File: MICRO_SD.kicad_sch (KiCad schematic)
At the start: 9 parts, among them J15 TF-028-H265

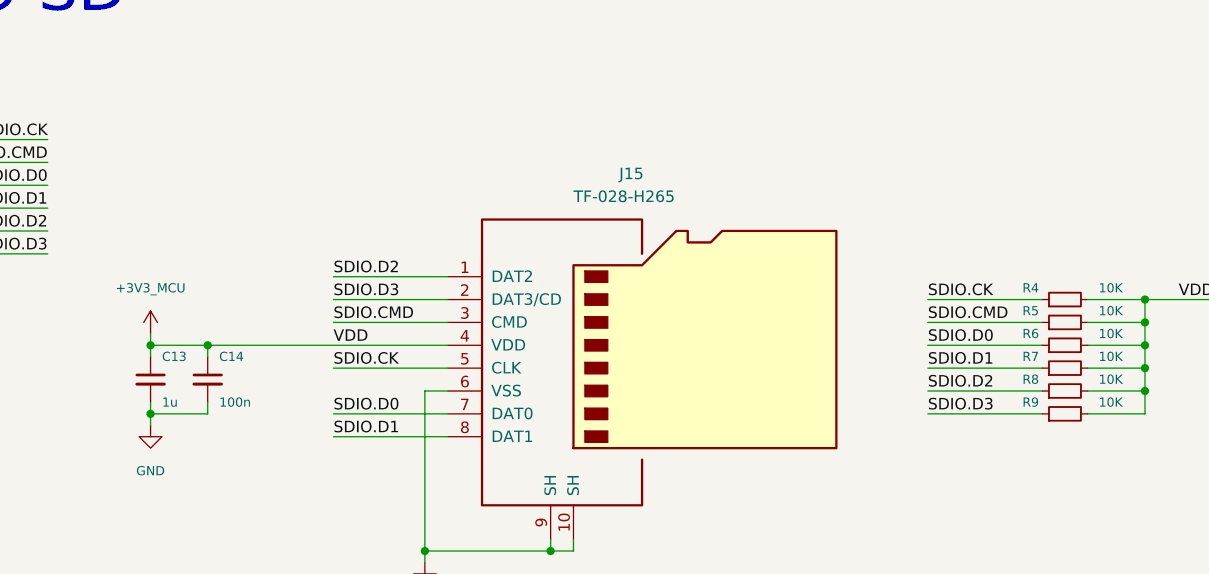
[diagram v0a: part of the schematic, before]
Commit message: grouped ICs and passives
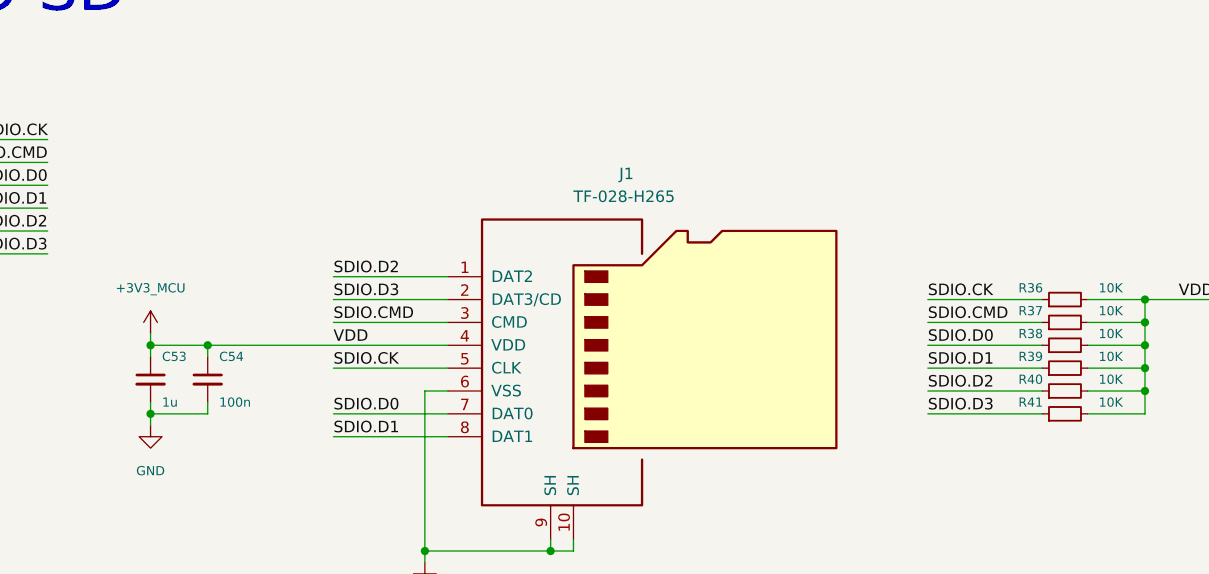
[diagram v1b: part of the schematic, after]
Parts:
- renumbered C13 to C53, C14 to C54, J15 to J1, R4 to R36, R5 to R37, R6 to R38, R7 to R39, R8 to R40, R9 to R41
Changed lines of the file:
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@@
 		(in_pos_files yes)
 		(dnp no)
-		(property "Reference" "R8"
+		(property "Reference" "R40"
 			(at 151.13 62.23 90)
 			(show_name no)
@@
 			(project "LEVIA_H7"
 				(path "/6b768b36-fce6-4be0-9021-6d41bddc3a70/f6fdd950-a71d-4aac-93a8-c5aad57c018b"
-					(reference "R8")
+					(reference "R40")
 					(unit 1)
 				)
@@
 		(in_pos_files yes)
 		(dnp no)
-		(property "Reference" "R7"
+		(property "Reference" "R39"
 			(at 151.13 59.69 90)
 			(show_name no)
@@
 			(project "LEVIA_H7"
 				(path "/6b768b36-fce6-4be0-9021-6d41bddc3a70/f6fdd950-a71d-4aac-93a8-c5aad57c018b"
-					(reference "R7")
+					(reference "R39")
 					(unit 1)
 				)
@@
 		(in_pos_files yes)
 		(dnp no)
-		(property "Reference" "R4"
+		(property "Reference" "R36"
 			(at 151.13 52.07 90)
 			(show_name no)
@@
 			(project "LEVIA_H7"
 				(path "/6b768b36-fce6-4be0-9021-6d41bddc3a70/f6fdd950-a71d-4aac-93a8-c5aad57c018b"
-					(reference "R4")
+					(reference "R36")
 					(unit 1)
 				)
@@
 		(dnp no)
 		(fields_autoplaced yes)
-		(property "Reference" "#PWR021"
+		(property "Reference" "#PWR0116"
 			(at 53.34 73.66 0)
 			(hide yes)
@@
 			(project "LEVIA_H7"
 				(path "/6b768b36-fce6-4be0-9021-6d41bddc3a70/f6fdd950-a71d-4aac-93a8-c5aad57c018b"
-					(reference "#PWR021")
+					(reference "#PWR0116")
 					(unit 1)
 				)
@@
 		(in_pos_files yes)
 		(dnp no)
-		(property "Reference" "R6"
+		(property "Reference" "R38"
 			(at 151.13 57.15 90)
 			(show_name no)
@@
 			(project "LEVIA_H7"
 				(path "/6b768b36-fce6-4be0-9021-6d41bddc3a70/f6fdd950-a71d-4aac-93a8-c5aad57c018b"
-					(reference "R6")
+					(reference "R38")
 					(unit 1)
 				)
@@
 		(in_pos_files yes)
 		(dnp no)
-		(property "Reference" "R5"
+		(property "Reference" "R37"
 			(at 151.13 54.61 90)
 			(show_name no)
@@
 			(project "LEVIA_H7"
 				(path "/6b768b36-fce6-4be0-9021-6d41bddc3a70/f6fdd950-a71d-4aac-93a8-c5aad57c018b"
-					(reference "R5")
+					(reference "R37")
 					(unit 1)
 				)
@@
 		(in_pos_files yes)
 		(dnp no)
-		(property "Reference" "C14"
+		(property "Reference" "C54"
 			(at 60.96 59.69 0)
 			(show_name no)
@@
 			(project "LEVIA_H7"
 				(path "/6b768b36-fce6-4be0-9021-6d41bddc3a70/f6fdd950-a71d-4aac-93a8-c5aad57c018b"
-					(reference "C14")
+					(reference "C54")
 					(unit 1)
 				)
@@
 		(in_pos_files yes)
 		(dnp no)
-		(property "Reference" "J15"
+		(property "Reference" "J1"
 			(at 105.41 39.37 0)
 			(show_name no)
@@
 			(project "LEVIA_H7"
 				(path "/6b768b36-fce6-4be0-9021-6d41bddc3a70/f6fdd950-a71d-4aac-93a8-c5aad57c018b"
-					(reference "J15")
+					(reference "J1")
 					(unit 1)
 				)
@@
 		(in_pos_files yes)
 		(dnp no)
-		(property "Reference" "C13"
+		(property "Reference" "C53"
 			(at 54.61 59.69 0)
 			(show_name no)
@@
 			(project "LEVIA_H7"
 				(path "/6b768b36-fce6-4be0-9021-6d41bddc3a70/f6fdd950-a71d-4aac-93a8-c5aad57c018b"
-					(reference "C13")
+					(reference "C53")
 					(unit 1)
 				)
@@
 		(in_pos_files yes)
 		(dnp no)
-		(property "Reference" "R9"
+		(property "Reference" "R41"
 			(at 151.13 64.77 90)
 			(show_name no)
@@
 			(project "LEVIA_H7"
 				(path "/6b768b36-fce6-4be0-9021-6d41bddc3a70/f6fdd950-a71d-4aac-93a8-c5aad57c018b"
-					(reference "R9")
+					(reference "R41")
 					(unit 1)
 				)
@@
 		(dnp no)
 		(fields_autoplaced yes)
-		(property "Reference" "#PWR020"
+		(property "Reference" "#PWR0115"
 			(at 53.34 60.96 0)
 			(hide yes)
@@
 			(project "LEVIA_H7"
 				(path "/6b768b36-fce6-4be0-9021-6d41bddc3a70/f6fdd950-a71d-4aac-93a8-c5aad57c018b"
-					(reference "#PWR020")
+					(reference "#PWR0115")
 					(unit 1)
 				)
@@
 		(dnp no)
 		(fields_autoplaced yes)
-		(property "Reference" "#PWR032"
+		(property "Reference" "#PWR0117"
 			(at 83.82 88.9 0)
 			(hide yes)
@@
 			(project "LEVIA_H7"
 				(path "/6b768b36-fce6-4be0-9021-6d41bddc3a70/f6fdd950-a71d-4aac-93a8-c5aad57c018b"
-					(reference "#PWR032")
-					(unit 1)
-				)
+					(reference "#PWR0117")
+					(unit 1)
+				)
